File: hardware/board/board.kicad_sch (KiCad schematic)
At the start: 38 parts, among them J1 Power, J10 OUT B3, J11 OUT B4, J2 IN A, J3 OUT A1, J4 OUT A2, J5 OUT A3, J6 OUT A4, J7 IN B, J8 OUT B1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

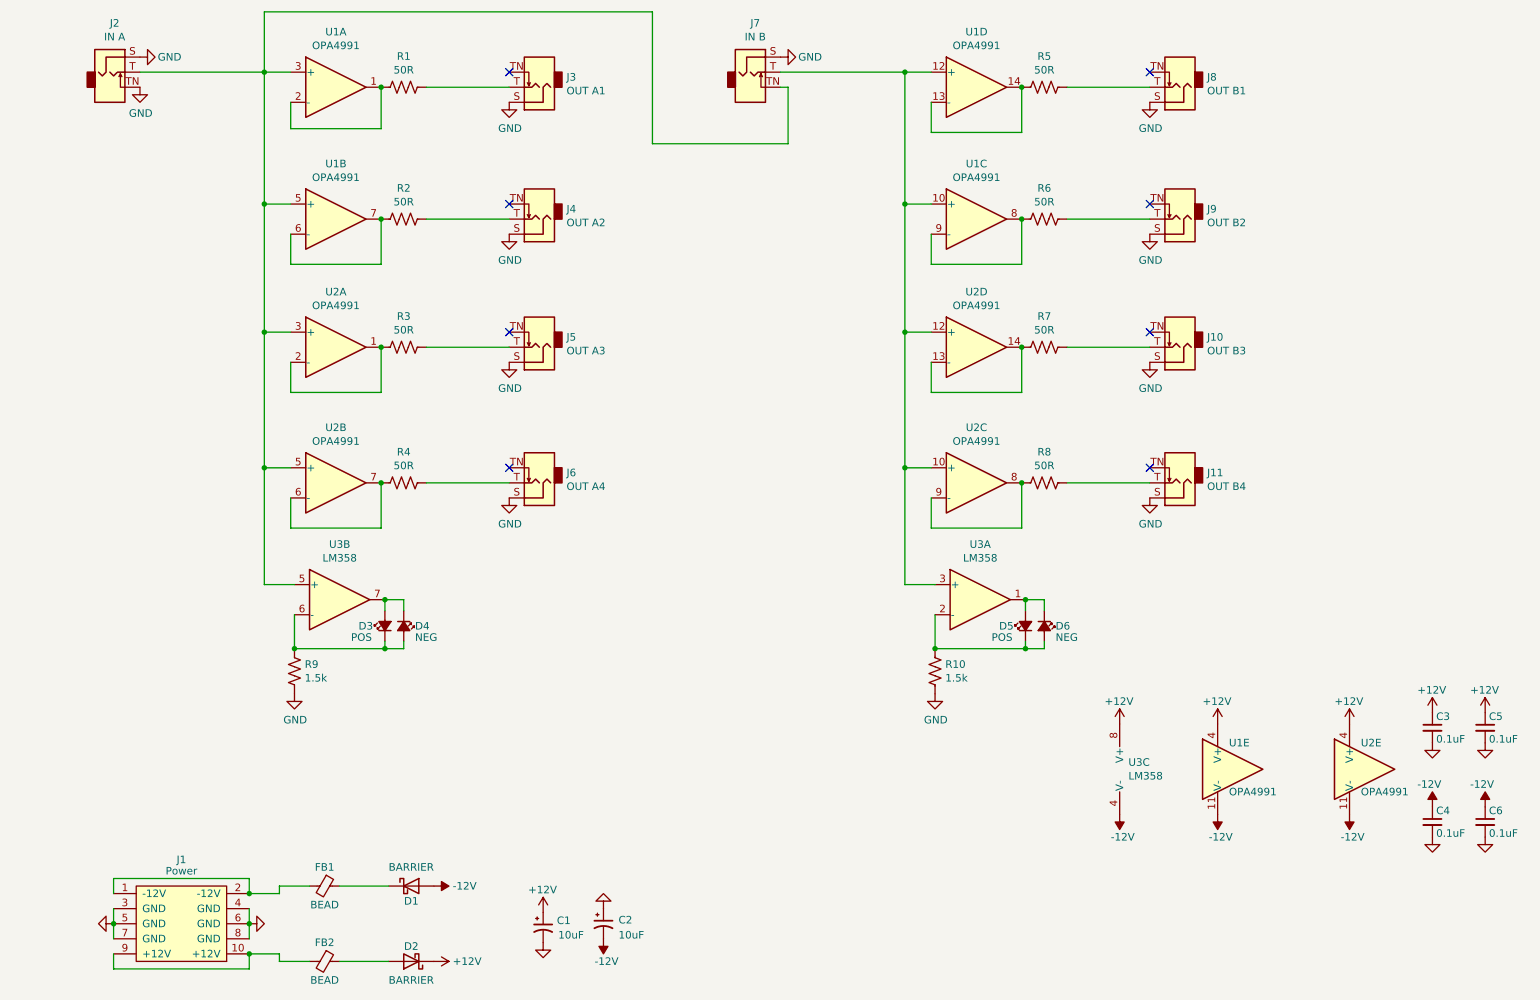
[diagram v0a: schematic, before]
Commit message: Board revision 3
Schematic:
- Migrated to new Winterbloom page layout
- Split into power and mult schematics
- Updated all symbols
- Added sourcing information for all items

PCB:
- Migrated to new Winterbloom page layout
- Updated all footprints
- Tweaked routing
- Updated all text to match current practices

Note:
- No values or placement locations were changed, this revision is largely cosmetic.
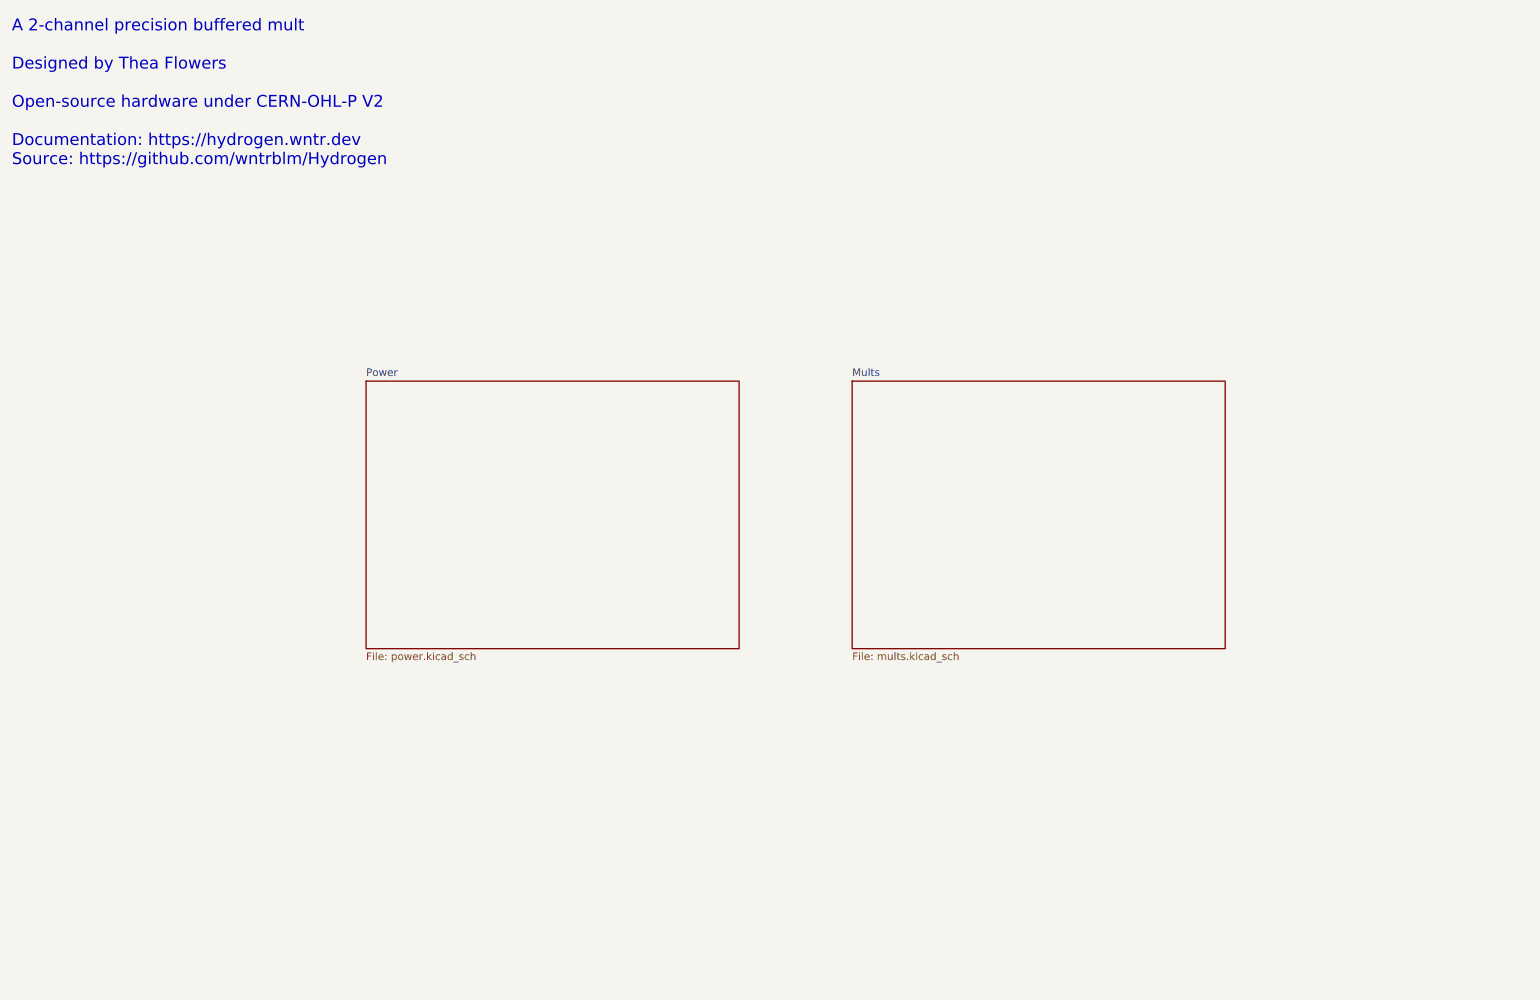
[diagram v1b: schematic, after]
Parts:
- removed C1, C2: 10uF, Capacitor_SMD:C_0805_2012Metric_Pad1.18x1.45mm_HandSolder, symbol Device:CP1_Small
- removed C3, C4, C5, C6: 0.1uF, Capacitor_SMD:C_0603_1608Metric_Pad1.08x0.95mm_HandSolder, symbol Device:C_Small
- removed D1, D2: BARRIER, winterbloom:DIODE_SOD-123_SOD-123F, symbol Diode:1N5819
- removed D3, D5: POS, winterbloom:LED_0805_Kingbright_APT2012, symbol Device:LED_Small_ALT
- removed D4, D6: NEG, winterbloom:LED_0805_Kingbright_APT2012, symbol Device:LED_Small_ALT
- removed FB1, FB2: BEAD, Inductor_SMD:L_0603_1608Metric_Pad1.05x0.95mm_HandSolder, symbol Device:Ferrite_Bead_Small
- removed J1: Power, winterbloom:Eurorack_Power, symbol board-rescue:Eurorack_Power-winterbloom
- removed J10: OUT B3, winterbloom:WQP-WQP518MA-skinny, symbol winterbloom:Eurorack_Mono_Jack
- removed J11: OUT B4, winterbloom:WQP-WQP518MA-skinny, symbol winterbloom:Eurorack_Mono_Jack
- removed J2: IN A, winterbloom:WQP-WQP518MA-skinny, symbol winterbloom:Eurorack_Mono_Jack
- removed J3: OUT A1, winterbloom:WQP-WQP518MA-skinny, symbol winterbloom:Eurorack_Mono_Jack
- removed J4: OUT A2, winterbloom:WQP-WQP518MA-skinny, symbol winterbloom:Eurorack_Mono_Jack
- removed J5: OUT A3, winterbloom:WQP-WQP518MA-skinny, symbol winterbloom:Eurorack_Mono_Jack
- removed J6: OUT A4, winterbloom:WQP-WQP518MA-skinny, symbol winterbloom:Eurorack_Mono_Jack
- removed J7: IN B, winterbloom:WQP-WQP518MA-skinny, symbol winterbloom:Eurorack_Mono_Jack
- removed J8: OUT B1, winterbloom:WQP-WQP518MA-skinny, symbol winterbloom:Eurorack_Mono_Jack
- removed J9: OUT B2, winterbloom:WQP-WQP518MA-skinny, symbol winterbloom:Eurorack_Mono_Jack
- removed R1, R2, R3, R4, R5, R6, R7, R8: 50R, Resistor_SMD:R_0603_1608Metric_Pad0.98x0.95mm_HandSolder, symbol Device:R_US
- removed R10, R9: 1.5k, Resistor_SMD:R_0603_1608Metric_Pad0.98x0.95mm_HandSolder, symbol Device:R_US
- removed U1, U2: OPA4991, Package_SO:TSSOP-14_4.4x5mm_P0.65mm, symbol winterbloom:OPA4991
- removed U3: LM358, Package_SO:TSSOP-8_4.4x3mm_P0.65mm, symbol Amplifier_Operational:LM358
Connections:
- no-connect marks 8 -> 0
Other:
- added sheet Mults (mults.kicad_sch)
- added sheet Power (power.kicad_sch)
- note added: "A 2-channel precision buffered mult Designed by Thea Flowers Open-source hardware under CERN-OHL-P V2 Documentation: https://hydrogen.wntr.dev Source: https://github.com/wntrblm/Hydrogen"
